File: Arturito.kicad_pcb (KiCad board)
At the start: 2 copper layers, 8 parts, among them IC1 L293D, J1 Alimentación, J2 Motor 1, J3 Motor 2, J4 Control_M1, J5 Control_M2

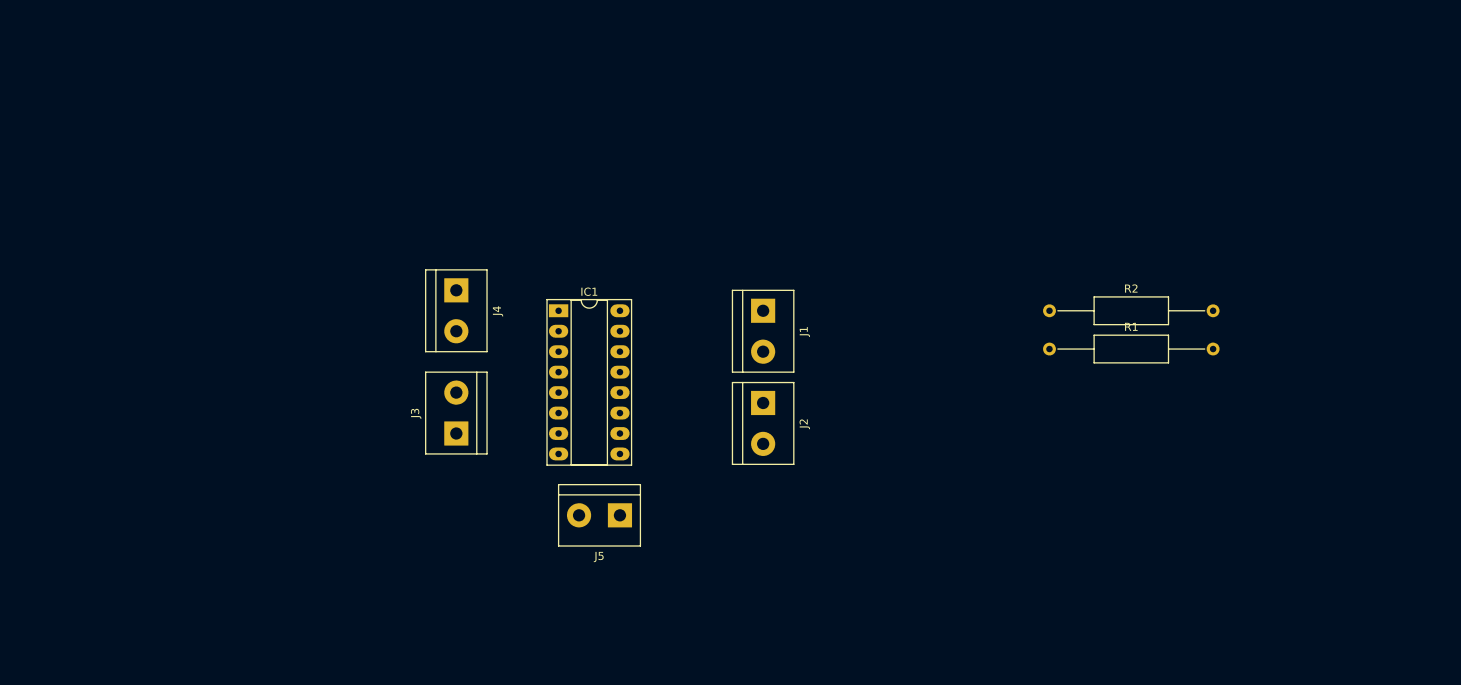
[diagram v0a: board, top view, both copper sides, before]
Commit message: Actualizado con huellas y materiales extra al diagrama
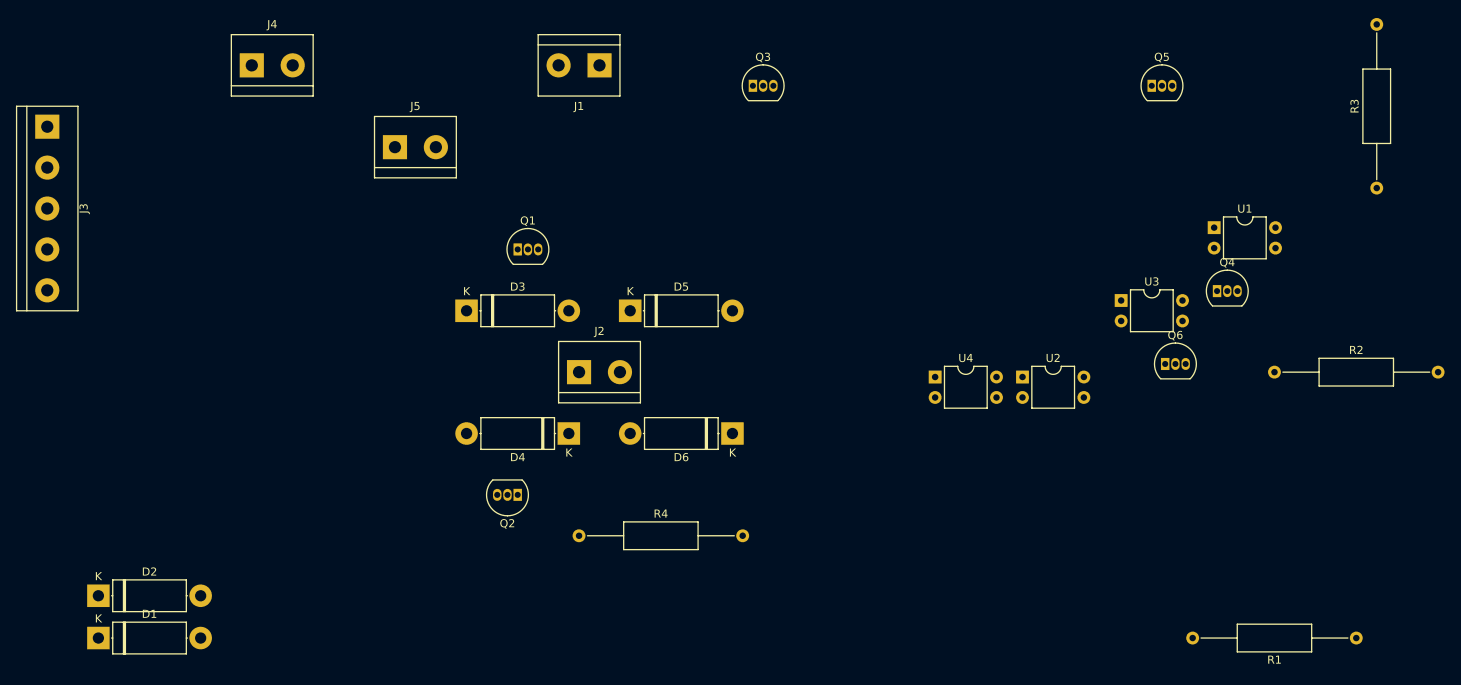
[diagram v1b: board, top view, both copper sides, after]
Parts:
- removed IC1: L293D, Package_DIP:DIP-16_W7.62mm_Socket_LongPads
- added D1: DIODE, Diode_THT:D_5W_P12.70mm_Horizontal, F.Cu at (80.0, 96.5)
- added D2: DIODE, Diode_THT:D_5W_P12.70mm_Horizontal, F.Cu at (80.0, 91.3)
- added D3: DIODE, Diode_THT:D_5W_P12.70mm_Horizontal, F.Cu at (125.7, 55.9)
- added D4: DIODE, Diode_THT:D_5W_P12.70mm_Horizontal, F.Cu at (138.4, 71.1)
- added D5: DIODE, Diode_THT:D_5W_P12.70mm_Horizontal, F.Cu at (146.1, 55.9)
- added D6: DIODE, Diode_THT:D_5W_P12.70mm_Horizontal, F.Cu at (158.8, 71.1)
- added Q1: 2N3904, Package_TO_SOT_THT:TO-92_Inline, F.Cu at (132.1, 48.3)
- added Q2: 2N3904, Package_TO_SOT_THT:TO-92_Inline, F.Cu at (132.1, 78.7)
- added Q3: 2N3904, Package_TO_SOT_THT:TO-92_Inline, F.Cu at (161.3, 27.9)
- added Q4: 2N3904, Package_TO_SOT_THT:TO-92_Inline, F.Cu at (218.9, 53.4)
- added Q5: 2n2222a, Package_TO_SOT_THT:TO-92_Inline, F.Cu at (210.8, 27.9)
- added Q6: 2n2222a, Package_TO_SOT_THT:TO-92_Inline, F.Cu at (212.5, 62.5)
- added R3: 1K, Resistor_THT:R_Axial_DIN0309_L9.0mm_D3.2mm_P20.32mm_Horizontal, F.Cu at (238.8, 40.6)
- added R4: 1K, Resistor_THT:R_Axial_DIN0309_L9.0mm_D3.2mm_P20.32mm_Horizontal, F.Cu at (139.7, 83.8)
- added U1: PC817, Package_DIP:DIP-4_W7.62mm, F.Cu at (218.6, 45.6)
- added U2: PC817, Package_DIP:DIP-4_W7.62mm, F.Cu at (194.8, 64.1)
- added U3: PC817, Package_DIP:DIP-4_W7.62mm, F.Cu at (207.0, 54.6)
- added U4: PC817, Package_DIP:DIP-4_W7.62mm, F.Cu at (183.9, 64.1)
- J3: value Motor 2 -> Conn_01x05; footprint TerminalBlock:TerminalBlock_bornier-2_P5.08mm -> TerminalBlock:TerminalBlock_bornier-5_P5.08mm
- R1, R2: value R_US -> 1K
- moved J3 63.5 mm to (73.7, 33.0), turned to -90 degrees
- moved J5 53.6 mm to (116.8, 35.6), turned to 0 degrees
- moved R1 52.3 mm to (236.2, 96.5), turned to 180 degrees
- moved J4 37.8 mm to (99.1, 25.4), turned to 0 degrees
- moved J1 36.6 mm to (142.2, 25.4), turned to 180 degrees
- moved R2 29.0 mm to (226.1, 63.5)
- moved J2 23.2 mm to (139.7, 63.5), turned to 0 degrees
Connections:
- J1 pad 1: +5V -> +9V
- J3 pad 1: Net-(J3-Pad1) -> /SL1
- J3 pad 2: Net-(J3-Pad2) -> /SL2
- R1 pad 1: unconnected-(R1-Pad1) -> Net-(R1-Pad1)
- R2 pad 1: Net-(R1-Pad2) -> Net-(R2-Pad1)
- R2 pad 2: unconnected-(R2-Pad2) -> Net-(R2-Pad2)

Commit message: Terminado DC,añadido stepper
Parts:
- removed D1, D2: DIODE, Diode_THT:D_5W_P12.70mm_Horizontal
- removed J4: Control_M1, TerminalBlock:TerminalBlock_bornier-2_P5.08mm
- removed J5: Control_M2, TerminalBlock:TerminalBlock_bornier-2_P5.08mm
- removed Q5, Q6: 2n2222a, Package_TO_SOT_THT:TO-92_Inline
- moved R4 79.7 mm to (180.3, 15.2)
- moved R3 60.4 mm to (180.3, 25.4), turned to 0 degrees
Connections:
- Q3 pad 1: Net-(Q4-Pad3) -> Net-(D5-Pad1)
- Q3 pad 2: unconnected-(Q3-Pad2) -> Net-(Q3-Pad2)
- Q4 pad 2: unconnected-(Q4-Pad2) -> Net-(Q4-Pad2)
- Q4 pad 3: Net-(Q4-Pad3) -> Net-(D5-Pad1)
- R1 pad 1: Net-(R1-Pad1) -> Net-(U2-Pad3)
- R3 pad 1: Net-(R3-Pad1) -> Net-(Q4-Pad2)
- R3 pad 2: Net-(Q5-Pad1) -> Net-(U4-Pad3)
- R4 pad 1: Net-(R4-Pad1) -> Net-(Q3-Pad2)
- R4 pad 2: Net-(Q6-Pad1) -> Net-(U3-Pad3)
- U1 pad 3: Net-(R3-Pad1) -> Net-(R2-Pad1)
- U2 pad 3: Net-(R4-Pad1) -> Net-(U2-Pad3)
- U3 pad 1: unconnected-(U3-Pad1) -> /SL3
- U3 pad 2: unconnected-(U3-Pad2) -> GND
- U3 pad 3: unconnected-(U3-Pad3) -> Net-(U3-Pad3)
- U3 pad 4: unconnected-(U3-Pad4) -> +9V
- U4 pad 1: unconnected-(U4-Pad1) -> /SL4
- U4 pad 2: unconnected-(U4-Pad2) -> GND
- U4 pad 3: unconnected-(U4-Pad3) -> Net-(U4-Pad3)
- U4 pad 4: unconnected-(U4-Pad4) -> +9V

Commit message: Casi terminado
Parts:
- added J4: Conn_01x03, TerminalBlock:TerminalBlock_bornier-3_P5.08mm, F.Cu at (109.2, 66.0)
- moved R1 128.3 mm to (108.0, 99.1), turned to -90 degrees
- moved R2 118.7 mm to (108.0, 74.9), turned to -90 degrees
- moved U1 100.3 mm to (120.7, 67.3), turned to -90 degrees
- moved R3 94.3 mm to (157.5, 116.8), turned to 90 degrees
- moved Q4 87.2 mm to (149.9, 106.7), turned to 90 degrees
- moved R4 80.8 mm to (157.5, 92.7), turned to 90 degrees
- moved U3 72.3 mm to (135.9, 67.3), turned to -90 degrees
- moved U2 66.6 mm to (128.3, 67.3), turned to -90 degrees
- moved Q3 60.8 mm to (149.9, 87.6), turned to 90 degrees
- moved J3 52.3 mm to (119.4, 58.4), turned to 0 degrees
- moved Q1 44.4 mm to (114.3, 88.9), turned to 90 degrees
- moved D4 43.9 mm to (121.9, 111.8), turned to 90 degrees
- moved D6 43.9 mm to (142.2, 111.8), turned to 90 degrees
- moved U4 40.5 mm to (143.5, 67.3), turned to -90 degrees
- moved J1 39.4 mm to (152.4, 63.5), turned to 90 degrees
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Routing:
- net +9V: track 0.00 -> 188.3 mm
- net GND: track 0.00 -> 133.6 mm
- net Net-(R1-Pad1): track 0.00 -> 48.5 mm
- net Net-(D5-Pad1): track 0.00 -> 35.5 mm
- net Net-(R3-Pad2): track 0.00 -> 35.0 mm
- net Net-(D3-Pad1): track 0.00 -> 33.5 mm
- net Net-(R4-Pad2): track 0.00 -> 25.2 mm
- net Net-(Q2-Pad2): track 0.00 -> 17.9 mm
- net Net-(Q4-Pad2): track 0.00 -> 16.1 mm
- net /SL4: track 0.00 -> 12.6 mm
- net Net-(Q3-Pad2): track 0.00 -> 11.7 mm
- net /SL3: track 0.00 -> 11.5 mm
- net Net-(Q1-Pad2): track 0.00 -> 11.2 mm
- net /SL2: track 0.00 -> 10.5 mm
- net Net-(R2-Pad1): track 0.00 -> 10.2 mm
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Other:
- board outline added: 63.5 x 73.7 mm

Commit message: final
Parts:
- added D3: DIODE, Diode_THT:D_5W_P12.70mm_Horizontal, F.Cu at (107.7, 139.1)
- added D3: DIODE, Diode_THT:D_5W_P12.70mm_Horizontal, F.Cu at (37.5, 139.3)
- added D3: DIODE, Diode_THT:D_5W_P12.70mm_Horizontal, F.Cu at (108.6, 61.7)
- added D3: DIODE, Diode_THT:D_5W_P12.70mm_Horizontal, F.Cu at (182.6, 136.3)
- added D3: DIODE, Diode_THT:D_5W_P12.70mm_Horizontal, F.Cu at (182.9, 61.5)
- added D4: DIODE, Diode_THT:D_5W_P12.70mm_Horizontal, F.Cu at (182.9, 79.2)
- added D4: DIODE, Diode_THT:D_5W_P12.70mm_Horizontal, F.Cu at (37.5, 157.1)
- added D4: DIODE, Diode_THT:D_5W_P12.70mm_Horizontal, F.Cu at (108.6, 79.5)
- added D4: DIODE, Diode_THT:D_5W_P12.70mm_Horizontal, F.Cu at (182.6, 154.1)
- added D4: DIODE, Diode_THT:D_5W_P12.70mm_Horizontal, F.Cu at (107.7, 156.8)
- added D5: DIODE, Diode_THT:D_5W_P12.70mm_Horizontal, F.Cu at (203.2, 60.2)
- added D5: DIODE, Diode_THT:D_5W_P12.70mm_Horizontal, F.Cu at (202.9, 135.0)
- added D5: DIODE, Diode_THT:D_5W_P12.70mm_Horizontal, F.Cu at (128.0, 137.8)
- added D5: DIODE, Diode_THT:D_5W_P12.70mm_Horizontal, F.Cu at (128.9, 60.5)
- added D5: DIODE, Diode_THT:D_5W_P12.70mm_Horizontal, F.Cu at (57.8, 138.0)
- added D6: DIODE, Diode_THT:D_5W_P12.70mm_Horizontal, F.Cu at (57.8, 157.1)
- added D6: DIODE, Diode_THT:D_5W_P12.70mm_Horizontal, F.Cu at (203.2, 79.2)
- added D6: DIODE, Diode_THT:D_5W_P12.70mm_Horizontal, F.Cu at (202.9, 154.1)
- added D6: DIODE, Diode_THT:D_5W_P12.70mm_Horizontal, F.Cu at (128.9, 79.5)
- added D6: DIODE, Diode_THT:D_5W_P12.70mm_Horizontal, F.Cu at (128.0, 156.8)
- added J1: Alimentación, TerminalBlock:TerminalBlock_bornier-2_P5.08mm, F.Cu at (138.2, 108.6)
- added J1: Alimentación, TerminalBlock:TerminalBlock_bornier-2_P5.08mm, F.Cu at (213.4, 31.0)
- added J1: Alimentación, TerminalBlock:TerminalBlock_bornier-2_P5.08mm, F.Cu at (67.9, 108.8)
- added J1: Alimentación, TerminalBlock:TerminalBlock_bornier-2_P5.08mm, F.Cu at (213.1, 105.8)
- added J1: Alimentación, TerminalBlock:TerminalBlock_bornier-2_P5.08mm, F.Cu at (139.1, 31.2)
- added J2: Motor 1, TerminalBlock:TerminalBlock_bornier-2_P5.08mm, F.Cu at (190.5, 55.1)
- added J2: Motor 1, TerminalBlock:TerminalBlock_bornier-2_P5.08mm, F.Cu at (115.3, 132.7)
- added J2: Motor 1, TerminalBlock:TerminalBlock_bornier-2_P5.08mm, F.Cu at (45.1, 133.0)
- added J2: Motor 1, TerminalBlock:TerminalBlock_bornier-2_P5.08mm, F.Cu at (190.2, 129.9)
- added J2: Motor 1, TerminalBlock:TerminalBlock_bornier-2_P5.08mm, F.Cu at (116.2, 55.4)
- added J3: Conn_01x05, TerminalBlock:TerminalBlock_bornier-5_P5.08mm, F.Cu at (180.3, 25.9)
- added J3: Conn_01x05, TerminalBlock:TerminalBlock_bornier-5_P5.08mm, F.Cu at (180.1, 100.7)
- added J3: Conn_01x05, TerminalBlock:TerminalBlock_bornier-5_P5.08mm, F.Cu at (105.2, 103.5)
- added J3: Conn_01x05, TerminalBlock:TerminalBlock_bornier-5_P5.08mm, F.Cu at (34.9, 103.8)
- added J3: Conn_01x05, TerminalBlock:TerminalBlock_bornier-5_P5.08mm, F.Cu at (106.0, 26.2)
- added J4: Conn_01x03, TerminalBlock:TerminalBlock_bornier-3_P5.08mm, F.Cu at (170.2, 33.5)
- added J4: Conn_01x03, TerminalBlock:TerminalBlock_bornier-3_P5.08mm, F.Cu at (24.8, 111.4)
- added J4: Conn_01x03, TerminalBlock:TerminalBlock_bornier-3_P5.08mm, F.Cu at (95.9, 33.8)
- added J4: Conn_01x03, TerminalBlock:TerminalBlock_bornier-3_P5.08mm, F.Cu at (169.9, 108.3)
- added J4: Conn_01x03, TerminalBlock:TerminalBlock_bornier-3_P5.08mm, F.Cu at (95.0, 111.1)
- added Q1: 2N3904, Package_TO_SOT_THT:TO-92_Inline, F.Cu at (175.0, 131.2)
- added Q1: 2N3904, Package_TO_SOT_THT:TO-92_Inline, F.Cu at (175.3, 56.4)
- added Q1: 2N3904, Package_TO_SOT_THT:TO-92_Inline, F.Cu at (101.0, 56.6)
- added Q1: 2N3904, Package_TO_SOT_THT:TO-92_Inline, F.Cu at (100.1, 134.0)
- added Q1: 2N3904, Package_TO_SOT_THT:TO-92_Inline, F.Cu at (29.8, 134.2)
- added Q2: 2N3904, Package_TO_SOT_THT:TO-92_Inline, F.Cu at (101.3, 151.8)
- added Q2: 2N3904, Package_TO_SOT_THT:TO-92_Inline, F.Cu at (102.2, 74.4)
- added Q2: 2N3904, Package_TO_SOT_THT:TO-92_Inline, F.Cu at (176.5, 74.2)
- added Q2: 2N3904, Package_TO_SOT_THT:TO-92_Inline, F.Cu at (31.1, 152.0)
- added Q2: 2N3904, Package_TO_SOT_THT:TO-92_Inline, F.Cu at (176.3, 149.0)
- added Q3: 2N3904, Package_TO_SOT_THT:TO-92_Inline, F.Cu at (65.4, 133.0)
- added Q3: 2N3904, Package_TO_SOT_THT:TO-92_Inline, F.Cu at (210.6, 129.9)
- added Q3: 2N3904, Package_TO_SOT_THT:TO-92_Inline, F.Cu at (135.6, 132.7)
- added Q3: 2N3904, Package_TO_SOT_THT:TO-92_Inline, F.Cu at (210.8, 55.1)
- added Q3: 2N3904, Package_TO_SOT_THT:TO-92_Inline, F.Cu at (136.5, 55.4)
- added Q4: 2N3904, Package_TO_SOT_THT:TO-92_Inline, F.Cu at (210.8, 74.2)
- added Q4: 2N3904, Package_TO_SOT_THT:TO-92_Inline, F.Cu at (136.5, 74.4)
- added Q4: 2N3904, Package_TO_SOT_THT:TO-92_Inline, F.Cu at (210.6, 149.0)
- added Q4: 2N3904, Package_TO_SOT_THT:TO-92_Inline, F.Cu at (65.4, 152.0)
- added Q4: 2N3904, Package_TO_SOT_THT:TO-92_Inline, F.Cu at (135.6, 151.8)
- added R1: 1K, Resistor_THT:R_Axial_DIN0309_L9.0mm_D3.2mm_P20.32mm_Horizontal, F.Cu at (93.7, 144.1)
- added R1: 1K, Resistor_THT:R_Axial_DIN0309_L9.0mm_D3.2mm_P20.32mm_Horizontal, F.Cu at (94.6, 66.8)
- added R1: 1K, Resistor_THT:R_Axial_DIN0309_L9.0mm_D3.2mm_P20.32mm_Horizontal, F.Cu at (168.7, 141.4)
- added R1: 1K, Resistor_THT:R_Axial_DIN0309_L9.0mm_D3.2mm_P20.32mm_Horizontal, F.Cu at (23.5, 144.4)
- added R1: 1K, Resistor_THT:R_Axial_DIN0309_L9.0mm_D3.2mm_P20.32mm_Horizontal, F.Cu at (168.9, 66.5)
- added R2: 1K, Resistor_THT:R_Axial_DIN0309_L9.0mm_D3.2mm_P20.32mm_Horizontal, F.Cu at (168.7, 117.2)
- added R2: 1K, Resistor_THT:R_Axial_DIN0309_L9.0mm_D3.2mm_P20.32mm_Horizontal, F.Cu at (23.5, 120.3)
- added R2: 1K, Resistor_THT:R_Axial_DIN0309_L9.0mm_D3.2mm_P20.32mm_Horizontal, F.Cu at (94.6, 42.7)
- added R2: 1K, Resistor_THT:R_Axial_DIN0309_L9.0mm_D3.2mm_P20.32mm_Horizontal, F.Cu at (93.7, 120.0)
- added R2: 1K, Resistor_THT:R_Axial_DIN0309_L9.0mm_D3.2mm_P20.32mm_Horizontal, F.Cu at (168.9, 42.4)
- added R3: 1K, Resistor_THT:R_Axial_DIN0309_L9.0mm_D3.2mm_P20.32mm_Horizontal, F.Cu at (144.1, 84.6)
- added R3: 1K, Resistor_THT:R_Axial_DIN0309_L9.0mm_D3.2mm_P20.32mm_Horizontal, F.Cu at (218.2, 159.1)
- added R3: 1K, Resistor_THT:R_Axial_DIN0309_L9.0mm_D3.2mm_P20.32mm_Horizontal, F.Cu at (73.0, 162.2)
- added R3: 1K, Resistor_THT:R_Axial_DIN0309_L9.0mm_D3.2mm_P20.32mm_Horizontal, F.Cu at (143.3, 161.9)
- added R3: 1K, Resistor_THT:R_Axial_DIN0309_L9.0mm_D3.2mm_P20.32mm_Horizontal, F.Cu at (218.4, 84.3)
- added R4: 1K, Resistor_THT:R_Axial_DIN0309_L9.0mm_D3.2mm_P20.32mm_Horizontal, F.Cu at (143.3, 137.8)
- added R4: 1K, Resistor_THT:R_Axial_DIN0309_L9.0mm_D3.2mm_P20.32mm_Horizontal, F.Cu at (73.0, 138.0)
- added R4: 1K, Resistor_THT:R_Axial_DIN0309_L9.0mm_D3.2mm_P20.32mm_Horizontal, F.Cu at (218.2, 135.0)
- added R4: 1K, Resistor_THT:R_Axial_DIN0309_L9.0mm_D3.2mm_P20.32mm_Horizontal, F.Cu at (144.1, 60.5)
- added R4: 1K, Resistor_THT:R_Axial_DIN0309_L9.0mm_D3.2mm_P20.32mm_Horizontal, F.Cu at (218.4, 60.2)
- added U1: PC817, Package_DIP:DIP-4_W7.62mm, F.Cu at (181.4, 109.6)
- added U1: PC817, Package_DIP:DIP-4_W7.62mm, F.Cu at (36.2, 112.6)
- added U1: PC817, Package_DIP:DIP-4_W7.62mm, F.Cu at (106.4, 112.4)
- added U1: PC817, Package_DIP:DIP-4_W7.62mm, F.Cu at (181.6, 34.8)
- added U1: PC817, Package_DIP:DIP-4_W7.62mm, F.Cu at (107.3, 35.0)
- added U2: PC817, Package_DIP:DIP-4_W7.62mm, F.Cu at (114.9, 35.1)
- added U2: PC817, Package_DIP:DIP-4_W7.62mm, F.Cu at (114.1, 112.4)
- added U2: PC817, Package_DIP:DIP-4_W7.62mm, F.Cu at (189.2, 34.8)
- added U2: PC817, Package_DIP:DIP-4_W7.62mm, F.Cu at (43.8, 112.7)
- added U2: PC817, Package_DIP:DIP-4_W7.62mm, F.Cu at (189.0, 109.6)
- added U3: PC817, Package_DIP:DIP-4_W7.62mm, F.Cu at (196.6, 109.6)
- added U3: PC817, Package_DIP:DIP-4_W7.62mm, F.Cu at (122.6, 35.1)
- added U3: PC817, Package_DIP:DIP-4_W7.62mm, F.Cu at (51.4, 112.7)
- added U3: PC817, Package_DIP:DIP-4_W7.62mm, F.Cu at (121.7, 112.4)
- added U3: PC817, Package_DIP:DIP-4_W7.62mm, F.Cu at (196.9, 34.8)
- added U4: PC817, Package_DIP:DIP-4_W7.62mm, F.Cu at (129.3, 112.4)
- added U4: PC817, Package_DIP:DIP-4_W7.62mm, F.Cu at (130.2, 35.0)
- added U4: PC817, Package_DIP:DIP-4_W7.62mm, F.Cu at (204.5, 34.8)
- added U4: PC817, Package_DIP:DIP-4_W7.62mm, F.Cu at (204.2, 109.6)
- added U4: PC817, Package_DIP:DIP-4_W7.62mm, F.Cu at (59.1, 112.6)
- moved D5 89.9 mm to (58.3, 60.4)
- moved D6 89.9 mm to (58.3, 79.5)
- moved J1 89.9 mm to (68.4, 31.2)
- moved Q3 89.9 mm to (65.9, 55.4)
- moved Q4 89.9 mm to (65.9, 74.4)
- moved R1 89.9 mm to (24.0, 66.8)
- moved R2 89.9 mm to (24.0, 42.7)
- moved U2 89.9 mm to (44.3, 35.1)
- moved U3 89.9 mm to (51.9, 35.1)
- moved U4 89.9 mm to (59.6, 35.0)
- moved D3 89.9 mm to (38.0, 61.7)
- moved D4 89.9 mm to (38.0, 79.5)
- moved J2 89.9 mm to (45.6, 55.4)
- moved J3 89.9 mm to (35.4, 26.2)
- moved J4 89.9 mm to (25.3, 33.8)
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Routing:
- net +9V: track 188.3 -> 1130.0 mm
- net GND: track 133.6 -> 801.4 mm
- net Net-(R1-Pad1): track 48.5 -> 290.8 mm
- net Net-(D5-Pad1): track 35.5 -> 213.1 mm
- net Net-(R3-Pad2): track 35.0 -> 209.9 mm
- net Net-(D3-Pad1): track 33.5 -> 201.1 mm
- net Net-(R4-Pad2): track 25.2 -> 151.1 mm
- net Net-(Q2-Pad2): track 17.9 -> 107.2 mm
- net Net-(Q4-Pad2): track 16.1 -> 96.4 mm
- net /SL4: track 12.6 -> 75.5 mm
- net Net-(Q3-Pad2): track 11.7 -> 70.4 mm
- net /SL3: track 11.5 -> 69.2 mm
- net Net-(Q1-Pad2): track 11.2 -> 66.9 mm
- net /SL2: track 10.5 -> 62.9 mm
- net Net-(R2-Pad1): track 10.2 -> 61.0 mm
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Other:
- board size 63.5 x 73.7 mm -> 208.9 x 151.5 mm
